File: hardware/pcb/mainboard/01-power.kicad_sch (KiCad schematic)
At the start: 42 parts, among them J1 BATTERIE JST-PH, J2 BOUTON contact JST-PH, J3 BOUTON LED JST-PH, Q1 AO3401A, Q2 2N7002, Q3 2N7002, SW1 QON, U2 BQ25896RTW, U3 TPS63001DRCR, U4 TPS61023DRL

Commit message: refactor(pcb): collapse to a single mainboard project
The two-perfboard design around the DevKitC-1 is gone; mainboard-v2 takes
the mainboard/ name and the -v2 suffix leaves every filename. The KiCad
project name is rewritten inside the instance blocks of all five sheets
too, otherwise KiCad drops the footprint assignments on open. ERC and DRC
still report 0 violations.

Add a Ground net class, split off Power, so GND carries its own via size
for the stitching and shows up in its own colour while routing. Its 0.2 mm
clearance is the neutral value: clearance resolves to the larger of the two
classes, so it never widens a gap on its own.

Drop the GPIO table from hardware/pcb/README.md rather than move it — the
netlist disagrees with it. PWR_HOLD no longer exists, PWR_SENSE is IO21 and
not IO41, and battery level comes from the BQ25896 over I2C instead of an
ADC. mainboard/README.md carries the pin plan that ships. wiring.md keeps
its bench-build pinout but stops attributing it to the deleted board.

hardware/bom.md, hardware/wiring.md and hardware/case/ still describe the
bench build, tracked as a TODO in the mainboard README.

Co-Authored-By: Claude Opus 5 <noreply@anthropic.com>
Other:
- title: Typoena mainboard v2 -> Typoena mainboard
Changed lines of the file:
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@@
 	(paper "A2")
 	(title_block
-		(title "Typoena mainboard v2")
+		(title "Typoena mainboard")
 		(date "2026-08-15")
 		(rev "A")
@@
 		)
 		(instances
-			(project "typoena-mainboard-v2"
+			(project "typoena-mainboard"
 				(path "/b1f0c5a2-7d34-4e19-9a6c-0f2e8d41c7b3/3a1c9e40-0001-4a00-9000-000000000001"
 					(reference "U2")
@@
 		)
 		(instances
-			(project "typoena-mainboard-v2"
+			(project "typoena-mainboard"
 				(path "/b1f0c5a2-7d34-4e19-9a6c-0f2e8d41c7b3/3a1c9e40-0001-4a00-9000-000000000001"
 					(reference "L1")
@@
 		)
 		(instances
-			(project "typoena-mainboard-v2"
+			(project "typoena-mainboard"
 				(path "/b1f0c5a2-7d34-4e19-9a6c-0f2e8d41c7b3/3a1c9e40-0001-4a00-9000-000000000001"
 					(reference "C1")
@@
 		)
 		(instances
-			(project "typoena-mainboard-v2"
+			(project "typoena-mainboard"
 				(path "/b1f0c5a2-7d34-4e19-9a6c-0f2e8d41c7b3/3a1c9e40-0001-4a00-9000-000000000001"
 					(reference "C2")
@@
 		)
 		(instances
-			(project "typoena-mainboard-v2"
+			(project "typoena-mainboard"
 				(path "/b1f0c5a2-7d34-4e19-9a6c-0f2e8d41c7b3/3a1c9e40-0001-4a00-9000-000000000001"
 					(reference "C3")
@@
 		)
 		(instances
-			(project "typoena-mainboard-v2"
+			(project "typoena-mainboard"
 				(path "/b1f0c5a2-7d34-4e19-9a6c-0f2e8d41c7b3/3a1c9e40-0001-4a00-9000-000000000001"
 					(reference "C4")
@@
 		)
 		(instances
-			(project "typoena-mainboard-v2"
+			(project "typoena-mainboard"
 				(path "/b1f0c5a2-7d34-4e19-9a6c-0f2e8d41c7b3/3a1c9e40-0001-4a00-9000-000000000001"
 					(reference "C5")
@@
 		)
 		(instances
-			(project "typoena-mainboard-v2"
+			(project "typoena-mainboard"
 				(path "/b1f0c5a2-7d34-4e19-9a6c-0f2e8d41c7b3/3a1c9e40-0001-4a00-9000-000000000001"
 					(reference "C6")
@@
 		)
 		(instances
-			(project "typoena-mainboard-v2"
+			(project "typoena-mainboard"
 				(path "/b1f0c5a2-7d34-4e19-9a6c-0f2e8d41c7b3/3a1c9e40-0001-4a00-9000-000000000001"
 					(reference "C7")
@@
 		)
 		(instances
-			(project "typoena-mainboard-v2"
+			(project "typoena-mainboard"
 				(path "/b1f0c5a2-7d34-4e19-9a6c-0f2e8d41c7b3/3a1c9e40-0001-4a00-9000-000000000001"
 					(reference "R1")
@@
 		)
 		(instances
-			(project "typoena-mainboard-v2"
+			(project "typoena-mainboard"
 				(path "/b1f0c5a2-7d34-4e19-9a6c-0f2e8d41c7b3/3a1c9e40-0001-4a00-9000-000000000001"
 					(reference "R2")
@@
 		)
 		(instances
-			(project "typoena-mainboard-v2"
+			(project "typoena-mainboard"
 				(path "/b1f0c5a2-7d34-4e19-9a6c-0f2e8d41c7b3/3a1c9e40-0001-4a00-9000-000000000001"
 					(reference "R3")
@@
 		)
 		(instances
-			(project "typoena-mainboard-v2"
+			(project "typoena-mainboard"
 				(path "/b1f0c5a2-7d34-4e19-9a6c-0f2e8d41c7b3/3a1c9e40-0001-4a00-9000-000000000001"
 					(reference "R4")
@@
 		)
 		(instances
-			(project "typoena-mainboard-v2"
+			(project "typoena-mainboard"
 				(path "/b1f0c5a2-7d34-4e19-9a6c-0f2e8d41c7b3/3a1c9e40-0001-4a00-9000-000000000001"
 					(reference "R5")
@@
 		)
 		(instances
-			(project "typoena-mainboard-v2"
+			(project "typoena-mainboard"
 				(path "/b1f0c5a2-7d34-4e19-9a6c-0f2e8d41c7b3/3a1c9e40-0001-4a00-9000-000000000001"
 					(reference "R6")
@@
 		)
 		(instances
-			(project "typoena-mainboard-v2"
+			(project "typoena-mainboard"
 				(path "/b1f0c5a2-7d34-4e19-9a6c-0f2e8d41c7b3/3a1c9e40-0001-4a00-9000-000000000001"
 					(reference "SW1")
@@
 		)
 		(instances
-			(project "typoena-mainboard-v2"
+			(project "typoena-mainboard"
 				(path "/b1f0c5a2-7d34-4e19-9a6c-0f2e8d41c7b3/3a1c9e40-0001-4a00-9000-000000000001"
 					(reference "D1")
@@
 		)
 		(instances
-			(project "typoena-mainboard-v2"
+			(project "typoena-mainboard"
 				(path "/b1f0c5a2-7d34-4e19-9a6c-0f2e8d41c7b3/3a1c9e40-0001-4a00-9000-000000000001"
 					(reference "J1")
@@
 		)
 		(instances
-			(project "typoena-mainboard-v2"
+			(project "typoena-mainboard"
 				(path "/b1f0c5a2-7d34-4e19-9a6c-0f2e8d41c7b3/3a1c9e40-0001-4a00-9000-000000000001"
 					(reference "U3")
@@
 		)
 		(instances
-			(project "typoena-mainboard-v2"
+			(project "typoena-mainboard"
 				(path "/b1f0c5a2-7d34-4e19-9a6c-0f2e8d41c7b3/3a1c9e40-0001-4a00-9000-000000000001"
 					(reference "L2")
@@
 		)
 		(instances
-			(project "typoena-mainboard-v2"
+			(project "typoena-mainboard"
 				(path "/b1f0c5a2-7d34-4e19-9a6c-0f2e8d41c7b3/3a1c9e40-0001-4a00-9000-000000000001"
 					(reference "C8")
@@
 		)
 		(instances
-			(project "typoena-mainboard-v2"
+			(project "typoena-mainboard"
 				(path "/b1f0c5a2-7d34-4e19-9a6c-0f2e8d41c7b3/3a1c9e40-0001-4a00-9000-000000000001"
 					(reference "C9")
@@
 		)
 		(instances
-			(project "typoena-mainboard-v2"
+			(project "typoena-mainboard"
 				(path "/b1f0c5a2-7d34-4e19-9a6c-0f2e8d41c7b3/3a1c9e40-0001-4a00-9000-000000000001"
 					(reference "C30")
@@
 		)
 		(instances
-			(project "typoena-mainboard-v2"
+			(project "typoena-mainboard"
 				(path "/b1f0c5a2-7d34-4e19-9a6c-0f2e8d41c7b3/3a1c9e40-0001-4a00-9000-000000000001"
 					(reference "U4")
@@
 		)
 		(instances
-			(project "typoena-mainboard-v2"
+			(project "typoena-mainboard"
 				(path "/b1f0c5a2-7d34-4e19-9a6c-0f2e8d41c7b3/3a1c9e40-0001-4a00-9000-000000000001"
 					(reference "L3")
@@
 		)
 		(instances
-			(project "typoena-mainboard-v2"
+			(project "typoena-mainboard"
 				(path "/b1f0c5a2-7d34-4e19-9a6c-0f2e8d41c7b3/3a1c9e40-0001-4a00-9000-000000000001"
 					(reference "C10")
@@
 		)
 		(instances
-			(project "typoena-mainboard-v2"
+			(project "typoena-mainboard"
 				(path "/b1f0c5a2-7d34-4e19-9a6c-0f2e8d41c7b3/3a1c9e40-0001-4a00-9000-000000000001"
 					(reference "C11")
@@
 		)
 		(instances
-			(project "typoena-mainboard-v2"
+			(project "typoena-mainboard"
 				(path "/b1f0c5a2-7d34-4e19-9a6c-0f2e8d41c7b3/3a1c9e40-0001-4a00-9000-000000000001"
 					(reference "C12")
@@
 		)
 		(instances
-			(project "typoena-mainboard-v2"
+			(project "typoena-mainboard"
 				(path "/b1f0c5a2-7d34-4e19-9a6c-0f2e8d41c7b3/3a1c9e40-0001-4a00-9000-000000000001"
 					(reference "R10")
@@
 		)
 		(instances
-			(project "typoena-mainboard-v2"
+			(project "typoena-mainboard"
 				(path "/b1f0c5a2-7d34-4e19-9a6c-0f2e8d41c7b3/3a1c9e40-0001-4a00-9000-000000000001"
 					(reference "R11")
@@
 		)
 		(instances
-			(project "typoena-mainboard-v2"
+			(project "typoena-mainboard"
 				(path "/b1f0c5a2-7d34-4e19-9a6c-0f2e8d41c7b3/3a1c9e40-0001-4a00-9000-000000000001"
 					(reference "R12")
@@
 		)
 		(instances
-			(project "typoena-mainboard-v2"
+			(project "typoena-mainboard"
 				(path "/b1f0c5a2-7d34-4e19-9a6c-0f2e8d41c7b3/3a1c9e40-0001-4a00-9000-000000000001"
 					(reference "Q1")
@@
 		)
 		(instances
-			(project "typoena-mainboard-v2"
+			(project "typoena-mainboard"
 				(path "/b1f0c5a2-7d34-4e19-9a6c-0f2e8d41c7b3/3a1c9e40-0001-4a00-9000-000000000001"
 					(reference "R13")
@@
 		)
 		(instances
-			(project "typoena-mainboard-v2"
+			(project "typoena-mainboard"
 				(path "/b1f0c5a2-7d34-4e19-9a6c-0f2e8d41c7b3/3a1c9e40-0001-4a00-9000-000000000001"
 					(reference "Q2")
@@
 		)
 		(instances
-			(project "typoena-mainboard-v2"
+			(project "typoena-mainboard"
 				(path "/b1f0c5a2-7d34-4e19-9a6c-0f2e8d41c7b3/3a1c9e40-0001-4a00-9000-000000000001"
 					(reference "R14")
@@
 		)
 		(instances
-			(project "typoena-mainboard-v2"
+			(project "typoena-mainboard"
 				(path "/b1f0c5a2-7d34-4e19-9a6c-0f2e8d41c7b3/3a1c9e40-0001-4a00-9000-000000000001"
 					(reference "C13")
@@
 		)
 		(instances
-			(project "typoena-mainboard-v2"
+			(project "typoena-mainboard"
 				(path "/b1f0c5a2-7d34-4e19-9a6c-0f2e8d41c7b3/3a1c9e40-0001-4a00-9000-000000000001"
 					(reference "J2")
@@
 		)
 		(instances
-			(project "typoena-mainboard-v2"
+			(project "typoena-mainboard"
 				(path "/b1f0c5a2-7d34-4e19-9a6c-0f2e8d41c7b3/3a1c9e40-0001-4a00-9000-000000000001"
 					(reference "R15")
@@
 		)
 		(instances
-			(project "typoena-mainboard-v2"
+			(project "typoena-mainboard"
 				(path "/b1f0c5a2-7d34-4e19-9a6c-0f2e8d41c7b3/3a1c9e40-0001-4a00-9000-000000000001"
 					(reference "J3")
@@
 		)
 		(instances
-			(project "typoena-mainboard-v2"
+			(project "typoena-mainboard"
 				(path "/b1f0c5a2-7d34-4e19-9a6c-0f2e8d41c7b3/3a1c9e40-0001-4a00-9000-000000000001"
 					(reference "R16")
@@
 		)
 		(instances
-			(project "typoena-mainboard-v2"
+			(project "typoena-mainboard"
 				(path "/b1f0c5a2-7d34-4e19-9a6c-0f2e8d41c7b3/3a1c9e40-0001-4a00-9000-000000000001"
 					(reference "Q3")
@@
 		)
 		(instances
-			(project "typoena-mainboard-v2"
+			(project "typoena-mainboard"
 				(path "/b1f0c5a2-7d34-4e19-9a6c-0f2e8d41c7b3/3a1c9e40-0001-4a00-9000-000000000001"
 					(reference "R17")
@@
 		)
 		(instances
-			(project "typoena-mainboard-v2"
+			(project "typoena-mainboard"
 				(path "/b1f0c5a2-7d34-4e19-9a6c-0f2e8d41c7b3/3a1c9e40-0001-4a00-9000-000000000001"
 					(reference "#FLG00")
@@
 		)
 		(instances
-			(project "typoena-mainboard-v2"
+			(project "typoena-mainboard"
 				(path "/b1f0c5a2-7d34-4e19-9a6c-0f2e8d41c7b3/3a1c9e40-0001-4a00-9000-000000000001"
 					(reference "#FLG01")
@@
 		)
 		(instances
-			(project "typoena-mainboard-v2"
+			(project "typoena-mainboard"
 				(path "/b1f0c5a2-7d34-4e19-9a6c-0f2e8d41c7b3/3a1c9e40-0001-4a00-9000-000000000001"
 					(reference "#FLG02")
@@
 		)
 		(instances
-			(project "typoena-mainboard-v2"
+			(project "typoena-mainboard"
 				(path "/b1f0c5a2-7d34-4e19-9a6c-0f2e8d41c7b3/3a1c9e40-0001-4a00-9000-000000000001"
 					(reference "#FLG03")
@@
 		)
 		(instances
-			(project "typoena-mainboard-v2"
+			(project "typoena-mainboard"
 				(path "/b1f0c5a2-7d34-4e19-9a6c-0f2e8d41c7b3/3a1c9e40-0001-4a00-9000-000000000001"
 					(reference "#FLG04")

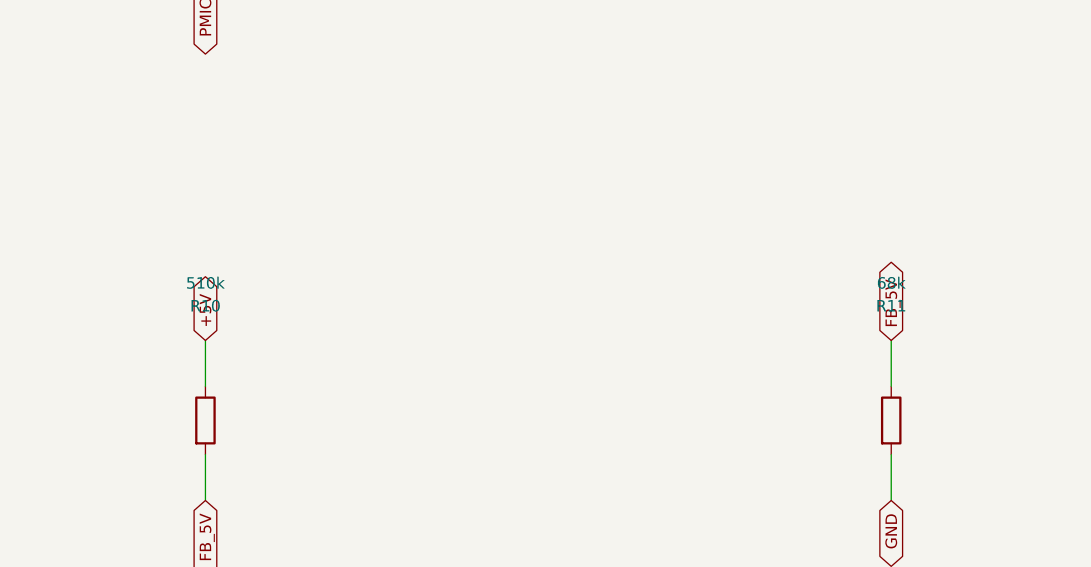
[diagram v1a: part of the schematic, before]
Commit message: fix(pcb): align the 5V feedback divider across schematic, BOM and notes
DESIGN-NOTES documented 750k/100k where the board carries 510k/68k. Same
7.5 ratio, same 5.06V out, but the notes described parts that do not exist.
Values now carry their 1% tolerance, which the ordered parts already had.

Co-Authored-By: Claude Opus 5 <noreply@anthropic.com>
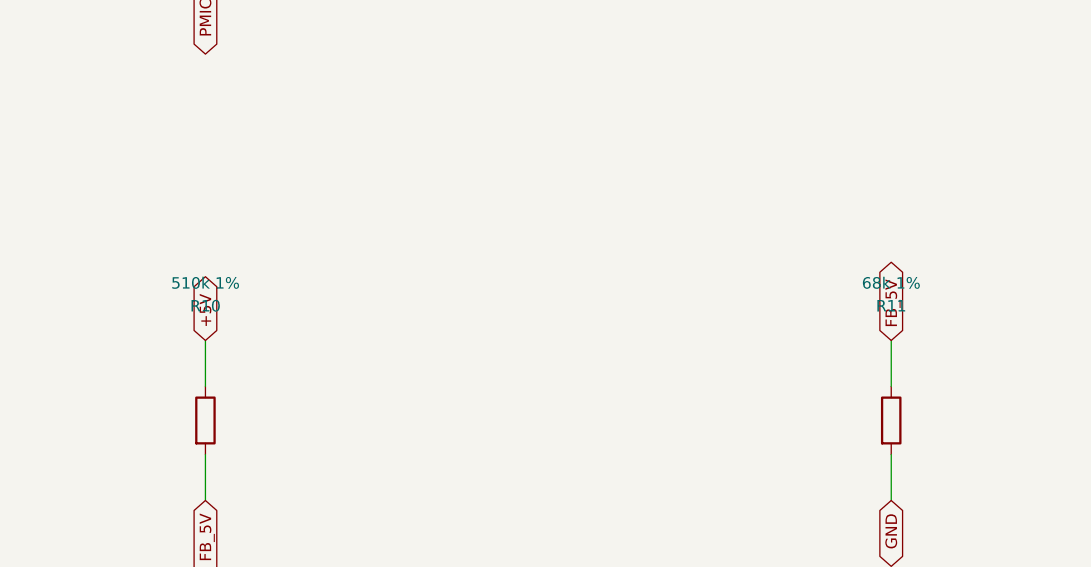
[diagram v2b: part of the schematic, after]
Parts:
- R10: value 510k -> 510k 1%
- R11: value 68k -> 68k 1%
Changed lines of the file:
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@@
 			)
 		)
-		(property "Value" "510k"
+		(property "Value" "510k 1%"
 			(at 63.5 182.88000000000002 0)
 			(effects
@@
 			)
 		)
-		(property "Value" "68k"
+		(property "Value" "68k 1%"
 			(at 139.7 182.88000000000002 0)
 			(effects

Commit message: feat(pcb): route the mainboard and add the design checker
801 segments, 110 vias, five filled zones, no unconnected net. Board is
94x45 mm with four #6-32 corner holes; D2 dropped and GPIO 48 exposed on
J10; J4 mechanical pin tied to GND.

tools/check_pcb.py consolidates the checks that were improvised until now:
switching-node discipline, hot loops, decoupling, via-in-pad, fine-pitch
escapes, current capacity, schematic/PCB cross-checks.

Co-Authored-By: Claude Opus 5 <noreply@anthropic.com>
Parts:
- R10: LCSC C11616 -> (none); MPN 0402WGF5103TCE -> (none)
- R11: LCSC C36871 -> (none); MPN 0402WGF6802TCE -> (none)

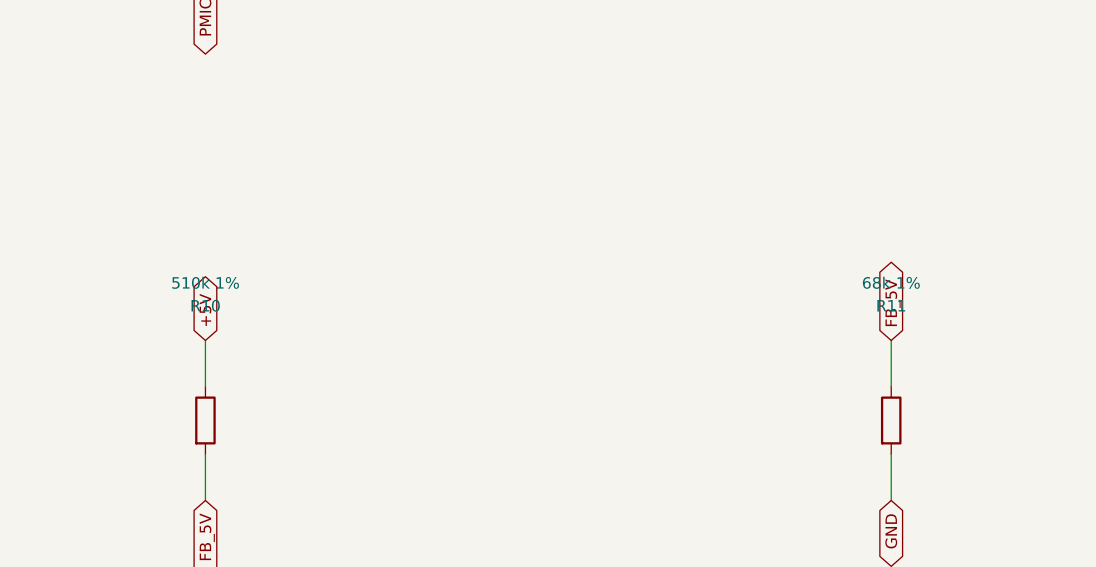
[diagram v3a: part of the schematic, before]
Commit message: fix(pcb): move the 5V feedback divider off the discontinued 68k
C36871 went out of stock, so the divider moves from 510k/68k to
56k/7.5k. The ratio holds at 7.5 either way, keeping VOUT at 5.04 V
against the 595 mV reference. The 56k is already on the board as the
USB-C CC pull-downs, so the swap adds one part number and drops two.

The divider draws 79 uA instead of 8.8, which the 5V rail being switched
off in sleep makes moot.

Both resistors also gain the LCSC and MPN fields they never had: the
lookup table in gen_sch.py keyed "68k" and "510k" while the schematic
declared "68k 1%" and "510k 1%", so neither ever matched and both would
have been left unpopulated. The table now carries the suffixed keys.

Co-Authored-By: Claude Opus 5 <noreply@anthropic.com>
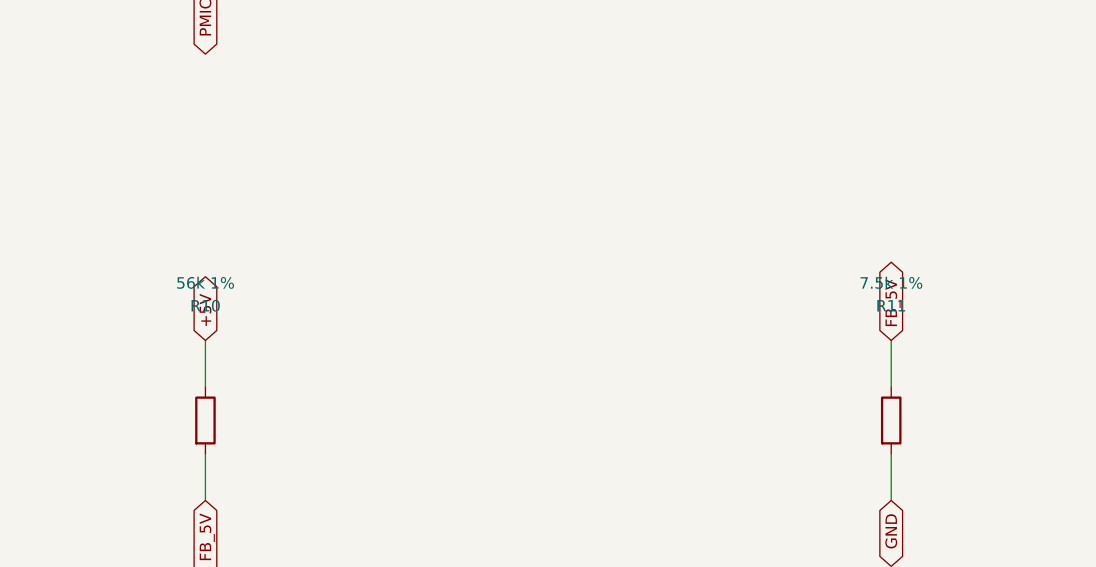
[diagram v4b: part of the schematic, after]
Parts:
- R10: value 510k 1% -> 56k 1%; LCSC (none) -> C25796; MPN (none) -> 0402WGF5602TCE
- R11: value 68k 1% -> 7.5k 1%; LCSC (none) -> C25918; MPN (none) -> 0402WGF7501TCE
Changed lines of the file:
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@@
 			)
 		)
-		(property "Value" "510k 1%"
+		(property "Value" "56k 1%"
 			(at 63.5 182.88 0)
 			(show_name no)
@@
 				)
 			)
-		)
-		(property "Footprint" "Resistor_SMD:R_0402_1005Metric"
+		)		(property "Footprint" "Resistor_SMD:R_0402_1005Metric"
 			(at 63.5 180.34 0)
 			(hide yes)
@@
 			)
 		)
-		(pin "1"
+		(property "LCSC" "C25796"
+			(at 63.5 172.72 0)
+			(hide yes)
+			(show_name no)
+			(do_not_autoplace no)
+			(effects
+				(font
+					(size 1.27 1.27)
+				)
+			)
+		)		(property "MPN" "0402WGF5602TCE"
+			(at 63.5 170.18 0)
+			(hide yes)
+			(show_name no)
+			(do_not_autoplace no)
+			(effects
+				(font
+					(size 1.27 1.27)
+				)
+			)
+		)	(pin "1"
 		)
 		(pin "2"
@@
 			)
 		)
-		(property "Value" "68k 1%"
+		(property "Value" "7.5k 1%"
 			(at 139.7 182.88 0)
 			(show_name no)
@@
 				)
 			)
-		)
-		(property "Footprint" "Resistor_SMD:R_0402_1005Metric"
+		)		(property "Footprint" "Resistor_SMD:R_0402_1005Metric"
 			(at 139.7 180.34 0)
 			(hide yes)
@@
 			)
 		)
-		(pin "1"
+		(property "LCSC" "C25918"
+			(at 139.7 172.72 0)
+			(hide yes)
+			(show_name no)
+			(do_not_autoplace no)
+			(effects
+				(font
+					(size 1.27 1.27)
+				)
+			)
+		)		(property "MPN" "0402WGF7501TCE"
+			(at 139.7 170.18 0)
+			(hide yes)
+			(show_name no)
+			(do_not_autoplace no)
+			(effects
+				(font
+					(size 1.27 1.27)
+				)
+			)
+		)	(pin "1"
 		)
 		(pin "2"
